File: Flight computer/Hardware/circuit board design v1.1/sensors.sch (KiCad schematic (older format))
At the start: 10 parts, among them U1 IIS2MDC, U10 BMI088, U8 MS5607-02BA

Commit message: put in new acclerometers and 9dof sensor. Changed supplier from mouser to farnell and RS
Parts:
- removed C28, C29, C31, C33: 100nF, Capacitor_SMD:C_0603_1608Metric, symbol Device:C_Small
- removed C30: 220nF, Capacitor_SMD:C_0603_1608Metric, symbol Device:C_Small
- removed C32: 10uF, Capacitor_SMD:C_0603_1608Metric, symbol Device:C_Small
- removed U1: IIS2MDC, Package_LGA:LGA-12_2x2mm_P0.5mm, symbol flight-computer:IIS2MDC
- removed U10: BMI088, BMI088:PQFN50P450X300X100-16N, symbol BMI088:BMI088
- added C13, C18: 10uF, Capacitor_SMD:C_0603_1608Metric, symbol Device:C_Small
- added C14, C15, C16, C17, C25: 100nF, Capacitor_SMD:C_0603_1608Metric, symbol Device:C_Small
- added C24: 10nF, Capacitor_SMD:C_0603_1608Metric, symbol Device:C_Small
- added U1: LSM9DS1, Package_LGA:LGA-24L_3x3.5mm_P0.43mm, symbol Sensor_Motion:LSM9DS1
- added U?: H3LIS100DL, Package_DFN_QFN:QFN-16-1EP_3x3mm_P0.5mm_EP1.45x1.45mm, symbol flight-computer:H3LIS100DL
- U8: min_quantity (none) -> 1
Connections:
- net labels added: ACCL_INT1, ACCL_INT2
- net labels removed: ACCL_RDY, GYRO_RDY, MAG_RDY
- wire segments 77 -> 113
- no-connect marks 4 -> 1
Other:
- note added: "C24(10nF) must guarantee \n1 nF value under 11 V bias \ncondition"
- note added: "Capacitor C1 (100 nF) should be a \ncapacitor with low ESR value and should \nbe placed as near as possible to the C1 pin."
- note added: "Power supply decoupling capacitors \n(100 nF ceramic, 10 μF aluminum) should be \nplaced as near as possible to pin 14 of the \ndevice (common design practice)."
- note added: "Power supply decoupling capacitors \n(100 nF ceramic,10 μF Al) should be placed \nas near as possible to the supply pin of the \ndevice (common design practice)."
- note added: "The slave address for accl/gyro is \n11010111b(D7h) for Read and \n11010110b (D6h) for Write."
- note added: "The slave address for mag is \n00111101b (3Dh) for Read and \n00111100b (3Ch) for Write."
- note added: "The slave address(SAD) is dress 0011001b.\nSA0 is connected to voltage supply."
- note removed: "Power supply decoupling capacitors (100 nF ceramic, 10 μF aluminum)"
- moved on the sheet: C77, U8

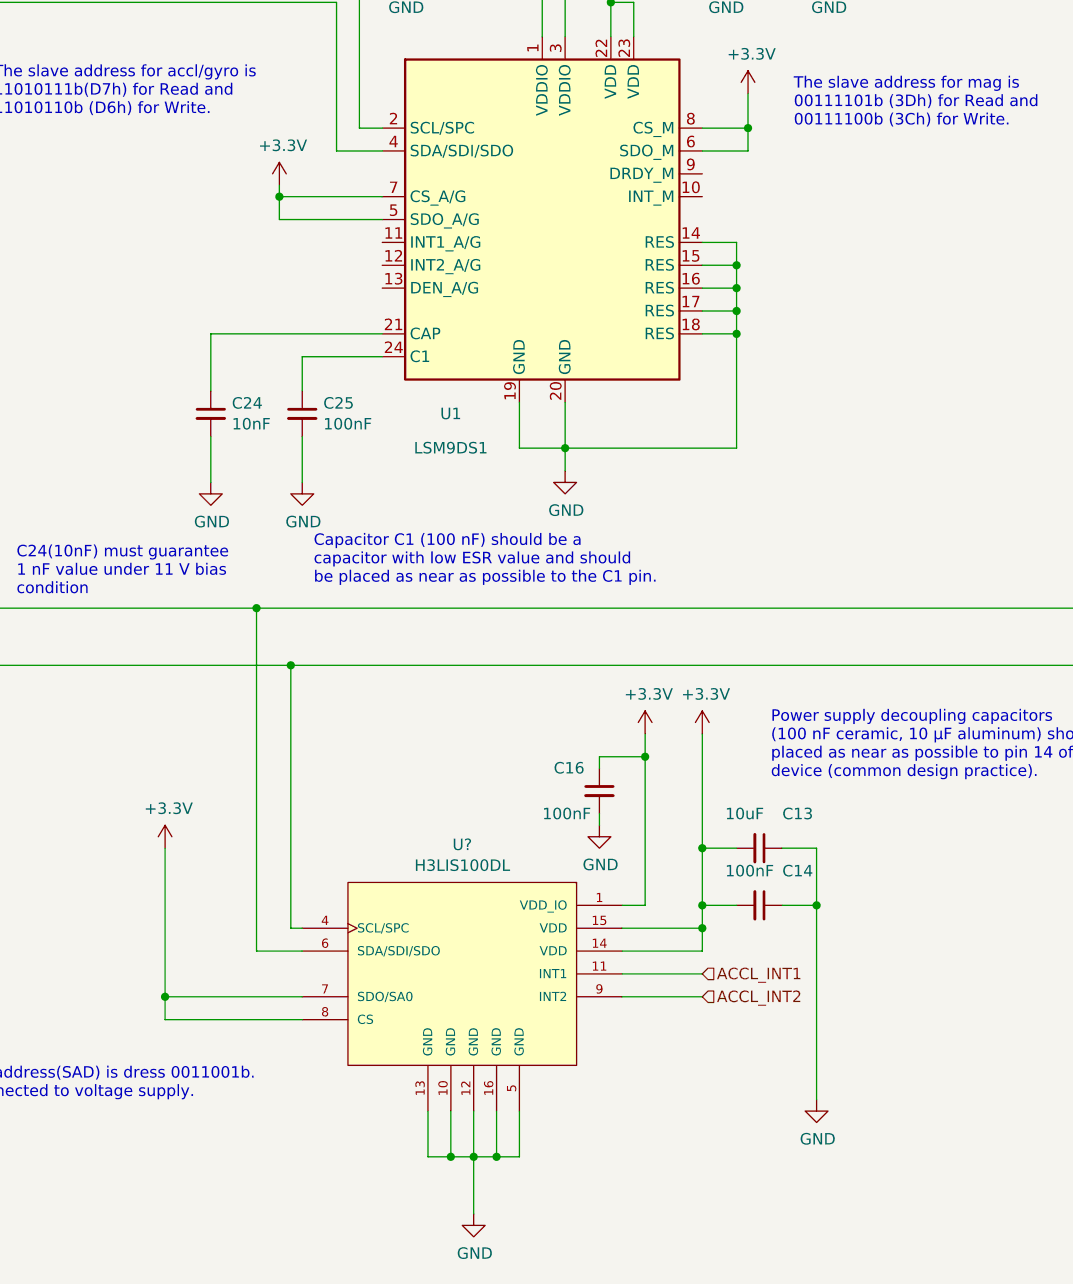
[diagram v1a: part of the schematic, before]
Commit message: wired up the news sensors
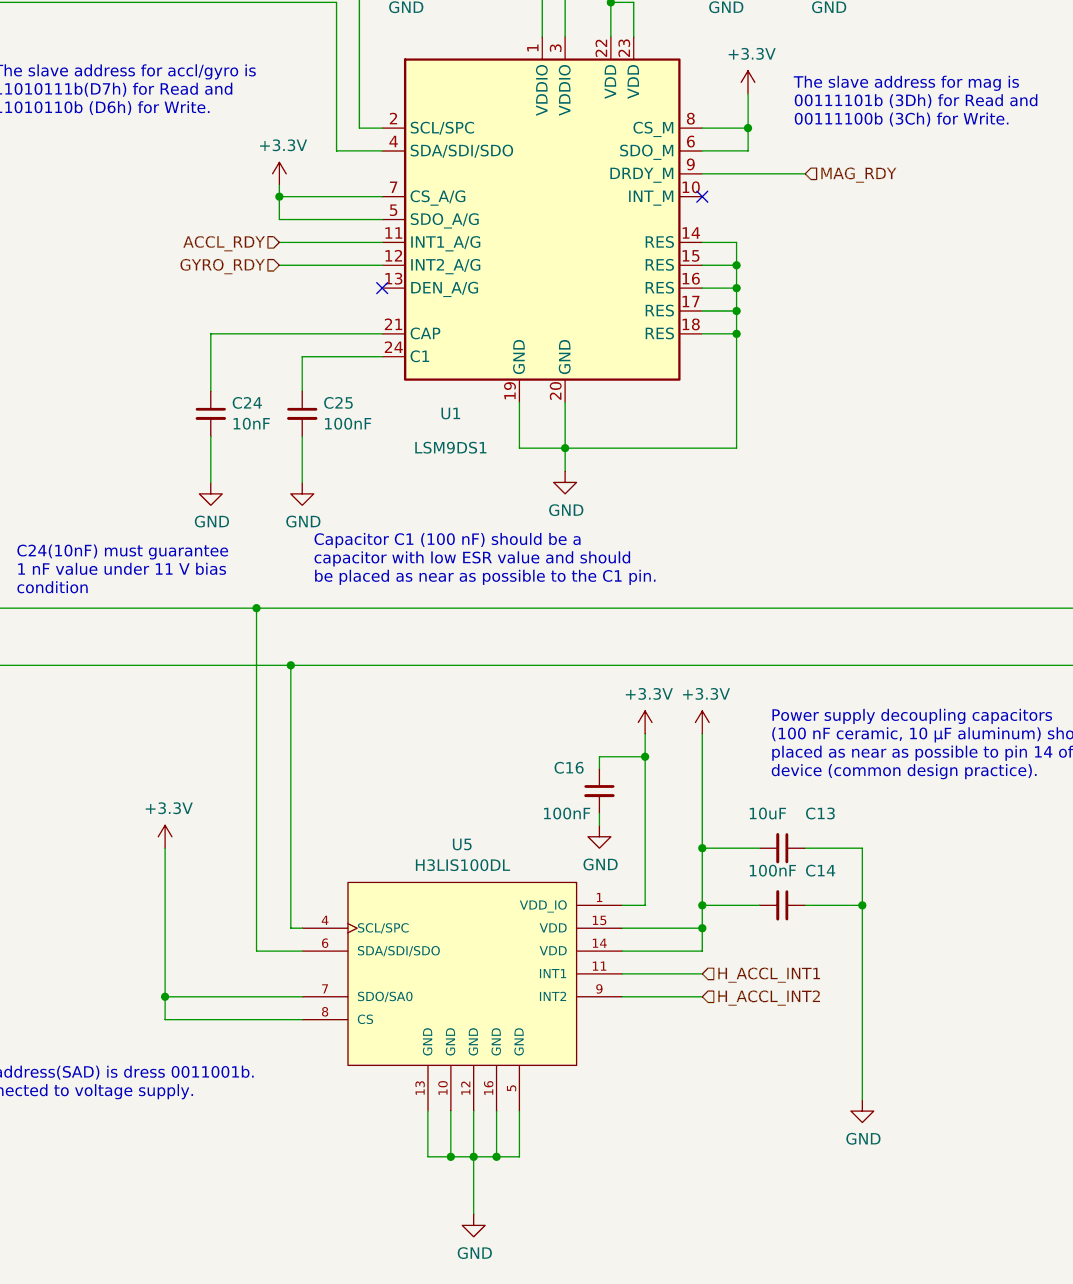
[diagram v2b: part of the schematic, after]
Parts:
- gave numbers to parts that had none: 1
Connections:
- net ACCL_RDY: now reaches U1.11 (INT1_A/G)
- net GYRO_RDY: now reaches U1.12 (INT2_A/G)
- net MAG_RDY: now reaches U1.9 (DRDY_M)
- net ACCL_INT1 renamed H_ACCL_INT1
- net ACCL_INT2 renamed H_ACCL_INT2
- no-connect marks 1 -> 3
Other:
- moved on the sheet: C13, C14
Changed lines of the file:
@@
 L power:GND #PWR017
 U 1 1 5D94C24A
-P 5700 6300
-F 0 "#PWR017" H 5700 6050 50  0001 C CNN
-F 1 "GND" H 5705 6127 50  0000 C CNN
-F 2 "" H 5700 6300 50  0001 C CNN
-F 3 "" H 5700 6300 50  0001 C CNN
-	1    5700 6300
+P 5900 6300
+F 0 "#PWR017" H 5900 6050 50  0001 C CNN
+F 1 "GND" H 5905 6127 50  0000 C CNN
+F 2 "" H 5900 6300 50  0001 C CNN
+F 3 "" H 5900 6300 50  0001 C CNN
+	1    5900 6300
 	1    0    0    -1
 $EndComp
@@
 L Device:C_Small C13
 U 1 1 5D94EBA2
-P 5450 5200
-F 0 "C13" V 5300 5300 50  0000 L CNN
-F 1 "10uF" V 5300 5050 50  0000 L CNN
-F 2 "Capacitor_SMD:C_0603_1608Metric" H 5450 5200 50  0001 C CNN
-F 3 "~" H 5450 5200 50  0001 C CNN
-	1    5450 5200
+P 5550 5200
+F 0 "C13" V 5400 5300 50  0000 L CNN
+F 1 "10uF" V 5400 5050 50  0000 L CNN
+F 2 "Capacitor_SMD:C_0603_1608Metric" H 5550 5200 50  0001 C CNN
+F 3 "~" H 5550 5200 50  0001 C CNN
+	1    5550 5200
 	0    1    1    0
 $EndComp
 Wire Wire Line
-	5200 5200 5350 5200
+	5200 5200 5450 5200
 Connection ~ 5200 5200
 Wire Wire Line
-	5550 5200 5700 5200
-Wire Wire Line
-	5700 5200 5700 5450
+	5650 5200 5900 5200
+Wire Wire Line
+	5900 5200 5900 5450
 $Comp
 L Device:C_Small C14
 U 1 1 5D951B11
-P 5450 5450
-F 0 "C14" V 5300 5550 50  0000 L CNN
-F 1 "100nF" V 5300 5300 50  0000 L CNN
-F 2 "Capacitor_SMD:C_0603_1608Metric" H 5450 5450 50  0001 C CNN
-F 3 "~" H 5450 5450 50  0001 C CNN
-	1    5450 5450
+P 5550 5450
+F 0 "C14" V 5400 5550 50  0000 L CNN
+F 1 "100nF" V 5400 5300 50  0000 L CNN
+F 2 "Capacitor_SMD:C_0603_1608Metric" H 5550 5450 50  0001 C CNN
+F 3 "~" H 5550 5450 50  0001 C CNN
+	1    5550 5450
 	0    1    1    0
 $EndComp
 Wire Wire Line
-	5200 5450 5350 5450
+	5200 5450 5450 5450
 Connection ~ 5200 5450
 Wire Wire Line
 	5200 5450 5200 5200
 Wire Wire Line
-	5550 5450 5700 5450
-Connection ~ 5700 5450
-Wire Wire Line
-	5700 5450 5700 6300
+	5650 5450 5900 5450
+Connection ~ 5900 5450
+Wire Wire Line
+	5900 5450 5900 6300
 Text Notes 5500 4900 0    50   ~ 0
 Power supply decoupling capacitors \n(100 nF ceramic, 10 μF aluminum) should be \nplaced as near as possible to pin 14 of the \ndevice (common design practice).
@@
 	4850 5450 4950 5450
 Text HLabel 5200 5750 2    50   Input ~ 0
-ACCL_INT1
+H_ACCL_INT1
 Wire Wire Line
 	4850 5750 5200 5750
 Text HLabel 5200 5850 2    50   Input ~ 0
-ACCL_INT2
+H_ACCL_INT2
 Wire Wire Line
 	5200 5850 4850 5850
@@
 C24(10nF) must guarantee \n1 nF value under 11 V bias \ncondition
 $Comp
-L flight-computer:H3LIS100DL U?
+L flight-computer:H3LIS100DL U5
 U 1 1 5D9FB40D
 P 4150 5750
-F 0 "U?" H 4150 6315 50  0000 C CNN
+F 0 "U5" H 4150 6315 50  0000 C CNN
 F 1 "H3LIS100DL" H 4150 6224 50  0000 C CNN
 F 2 "Package_DFN_QFN:QFN-16-1EP_3x3mm_P0.5mm_EP1.45x1.45mm" H 3550 6550 50  0001 L BNN
@@
 	3350 2350 3350 2300
 $Comp
-L power:+3.3V #PWR?
+L power:+3.3V #PWR046
 U 1 1 5DA31C3E
 P 3350 2300
-F 0 "#PWR?" H 3350 2150 50  0001 C CNN
+F 0 "#PWR046" H 3350 2150 50  0001 C CNN
 F 1 "+3.3V" H 3365 2473 50  0000 C CNN
 F 2 "" H 3350 2300 50  0001 C CNN
@@
 	5400 2050 5400 1900
 $Comp
-L power:+3.3V #PWR?
+L power:+3.3V #PWR047
 U 1 1 5DA4DC9B
 P 5400 1900
-F 0 "#PWR?" H 5400 1750 50  0001 C CNN
+F 0 "#PWR047" H 5400 1750 50  0001 C CNN
 F 1 "+3.3V" H 5415 2073 50  0000 C CNN
 F 2 "" H 5400 1900 50  0001 C CNN
@@
 Text Notes 5600 2050 0    50   ~ 0
 The slave address for mag is \n00111101b (3Dh) for Read and \n00111100b (3Ch) for Write.
+NoConn ~ 3800 2750
+Text HLabel 3350 2550 0    50   Input ~ 0
+ACCL_RDY
+Wire Wire Line
+	3800 2550 3350 2550
+Text HLabel 3350 2650 0    50   Input ~ 0
+GYRO_RDY
+Wire Wire Line
+	3800 2650 3350 2650
+Text HLabel 5650 2250 2    50   Input ~ 0
+MAG_RDY
+Wire Wire Line
+	5200 2250 5650 2250
+NoConn ~ 5200 2350
 $EndSCHEMATC

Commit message: Fully routed board v1.1 with the new high g accelerometer
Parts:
- U5: footprint Package_DFN_QFN:QFN-16-1EP_3x3mm_P0.5mm_EP1.45x1.45mm -> flight-computer:TFLGA-16_3x3mm
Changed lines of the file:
@@
 F 0 "U5" H 4150 6315 50  0000 C CNN
 F 1 "H3LIS100DL" H 4150 6224 50  0000 C CNN
-F 2 "Package_DFN_QFN:QFN-16-1EP_3x3mm_P0.5mm_EP1.45x1.45mm" H 3550 6550 50  0001 L BNN
+F 2 "flight-computer:TFLGA-16_3x3mm" H 3550 6550 50  0001 L BNN
 F 3 "https://docs-emea.rs-online.com/webdocs/14da/0900766b814da09a.pdf" H 3550 6550 50  0001 L BNN
 F 4 "2.47" H 4150 5750 50  0001 C CNN "Cost"

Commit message: put in logo for V1.1
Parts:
- C13, C18: Cost (none) -> 0.07; Purchase link (none) -> https://uk.rs-online.com/web/p/mlccs-multilayer-ceramic-cap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; min_quantity (none) -> 100
- C14, C15, C16, C17, C25: Cost (none) -> 0.01; Purchase link (none) -> https://uk.rs-online.com/web/p/mlccs-multilayer-ceramic-cap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; min_quantity (none) -> 50
- C24: Cost (none) -> 0.031; Purchase link (none) -> https://uk.rs-online.com/web/p/mlccs-multilayer-ceramic-cap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; min_quantity (none) -> 100
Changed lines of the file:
@@
 F 1 "10uF" V 5400 5050 50  0000 L CNN
 F 2 "Capacitor_SMD:C_0603_1608Metric" H 5550 5200 50  0001 C CNN
-F 3 "~" H 5550 5200 50  0001 C CNN
+F 3 "https://docs-emea.rs-online.com/webdocs/13b3/0900766b813b3e64.pdf" H 5550 5200 50  0001 C CNN
+F 4 "0.07" H 5550 5200 50  0001 C CNN "Cost"
+F 5 "https://uk.rs-online.com/web/p/mlccs-multilayer-ceramic-capacitors/8467293/" H 5550 5200 50  0001 C CNN "Purchase link"
+F 6 "100" H 5550 5200 50  0001 C CNN "min_quantity"
 	1    5550 5200
 	0    1    1    0
@@
 F 1 "100nF" V 5400 5300 50  0000 L CNN
 F 2 "Capacitor_SMD:C_0603_1608Metric" H 5550 5450 50  0001 C CNN
-F 3 "~" H 5550 5450 50  0001 C CNN
+F 3 "https://docs-emea.rs-online.com/webdocs/0dc2/0900766b80dc2409.pdf" H 5550 5450 50  0001 C CNN
+F 4 "0.01" H 5550 5450 50  0001 C CNN "Cost"
+F 5 "https://uk.rs-online.com/web/p/mlccs-multilayer-ceramic-capacitors/6983251/" H 5550 5450 50  0001 C CNN "Purchase link"
+F 6 "50" H 5550 5450 50  0001 C CNN "min_quantity"
 	1    5550 5450
 	0    1    1    0
@@
 F 1 "100nF" H 3992 1155 50  0000 L CNN
 F 2 "Capacitor_SMD:C_0603_1608Metric" H 3900 1200 50  0001 C CNN
-F 3 "~" H 3900 1200 50  0001 C CNN
+F 3 "https://docs-emea.rs-online.com/webdocs/0dc2/0900766b80dc2409.pdf" H 3900 1200 50  0001 C CNN
+F 4 "0.01" H 3900 1200 50  0001 C CNN "Cost"
+F 5 "https://uk.rs-online.com/web/p/mlccs-multilayer-ceramic-capacitors/6983251/" H 3900 1200 50  0001 C CNN "Purchase link"
+F 6 "50" H 3900 1200 50  0001 C CNN "min_quantity"
 	1    3900 1200
 	1    0    0    -1
@@
 F 1 "100nF" H 4500 4850 50  0000 L CNN
 F 2 "Capacitor_SMD:C_0603_1608Metric" H 4750 4950 50  0001 C CNN
-F 3 "~" H 4750 4950 50  0001 C CNN
+F 3 "https://docs-emea.rs-online.com/webdocs/0dc2/0900766b80dc2409.pdf" H 4750 4950 50  0001 C CNN
+F 4 "0.01" H 4750 4950 50  0001 C CNN "Cost"
+F 5 "https://uk.rs-online.com/web/p/mlccs-multilayer-ceramic-capacitors/6983251/" H 4750 4950 50  0001 C CNN "Purchase link"
+F 6 "50" H 4750 4950 50  0001 C CNN "min_quantity"
 	1    4750 4950
 	1    0    0    -1
@@
 F 1 "100nF" H 5392 1105 50  0000 L CNN
 F 2 "Capacitor_SMD:C_0603_1608Metric" H 5300 1150 50  0001 C CNN
-F 3 "~" H 5300 1150 50  0001 C CNN
+F 3 "https://docs-emea.rs-online.com/webdocs/0dc2/0900766b80dc2409.pdf" H 5300 1150 50  0001 C CNN
+F 4 "0.01" H 5300 1150 50  0001 C CNN "Cost"
+F 5 "https://uk.rs-online.com/web/p/mlccs-multilayer-ceramic-capacitors/6983251/" H 5300 1150 50  0001 C CNN "Purchase link"
+F 6 "50" H 5300 1150 50  0001 C CNN "min_quantity"
 	1    5300 1150
 	1    0    0    -1
@@
 F 1 "10uF" H 5842 1105 50  0000 L CNN
 F 2 "Capacitor_SMD:C_0603_1608Metric" H 5750 1150 50  0001 C CNN
-F 3 "~" H 5750 1150 50  0001 C CNN
+F 3 "https://docs-emea.rs-online.com/webdocs/13b3/0900766b813b3e64.pdf" H 5750 1150 50  0001 C CNN
+F 4 "0.07" H 5750 1150 50  0001 C CNN "Cost"
+F 5 "https://uk.rs-online.com/web/p/mlccs-multilayer-ceramic-capacitors/8467293/" H 5750 1150 50  0001 C CNN "Purchase link"
+F 6 "100" H 5750 1150 50  0001 C CNN "min_quantity"
 	1    5750 1150
 	1    0    0    -1
@@
 F 2 "Capacitor_SMD:C_0603_1608Metric" H 3050 3300 50  0001 C CNN
 F 3 "~" H 3050 3300 50  0001 C CNN
+F 4 "0.031" H 3050 3300 50  0001 C CNN "Cost"
+F 5 "https://uk.rs-online.com/web/p/mlccs-multilayer-ceramic-capacitors/8391727/" H 3050 3300 50  0001 C CNN "Purchase link"
+F 6 "100" H 3050 3300 50  0001 C CNN "min_quantity"
 	1    3050 3300
 	1    0    0    -1
@@
 F 1 "100nF" H 3542 3255 50  0000 L CNN
 F 2 "Capacitor_SMD:C_0603_1608Metric" H 3450 3300 50  0001 C CNN
-F 3 "~" H 3450 3300 50  0001 C CNN
+F 3 "https://docs-emea.rs-online.com/webdocs/0dc2/0900766b80dc2409.pdf" H 3450 3300 50  0001 C CNN
+F 4 "0.01" H 3450 3300 50  0001 C CNN "Cost"
+F 5 "https://uk.rs-online.com/web/p/mlccs-multilayer-ceramic-capacitors/6983251/" H 3450 3300 50  0001 C CNN "Purchase link"
+F 6 "50" H 3450 3300 50  0001 C CNN "min_quantity"
 	1    3450 3300
 	1    0    0    -1

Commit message: added in grove connector for break out pins. Made a new software framework for SAMD
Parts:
- added R4, R8: 4.7K, Resistor_SMD:R_0603_1608Metric, symbol Device:R
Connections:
- net +3V3: now also R4.1, R8.1
- net SENS_SCL: now also R8.2
- net SENS_SDA: now also R4.2
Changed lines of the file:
@@
 Connection ~ 3400 4400
 Wire Wire Line
-	3400 4400 8700 4400
+	3400 4400 7800 4400
 Wire Wire Line
 	3450 5650 3250 5650
@@
 Connection ~ 3250 4150
 Wire Wire Line
-	3250 4150 8850 4150
+	3250 4150 7500 4150
 Wire Wire Line
 	4850 5550 5200 5550
@@
 	5200 2250 5650 2250
 NoConn ~ 5200 2350
+Wire Wire Line
+	7500 3100 7500 3450
+Connection ~ 7500 4150
+Wire Wire Line
+	7500 4150 8850 4150
+Wire Wire Line
+	7800 4400 7800 3750
+Connection ~ 7800 4400
+Wire Wire Line
+	7800 4400 8700 4400
+$Comp
+L power:+3.3V #PWR048
+U 1 1 5D93D3F3
+P 7500 3100
+F 0 "#PWR048" H 7500 2950 50  0001 C CNN
+F 1 "+3.3V" H 7515 3273 50  0000 C CNN
+F 2 "" H 7500 3100 50  0001 C CNN
+F 3 "" H 7500 3100 50  0001 C CNN
+	1    7500 3100
+	1    0    0    -1
+$EndComp
+$Comp
+L power:+3.3V #PWR049
+U 1 1 5D93D8A4
+P 7800 3100
+F 0 "#PWR049" H 7800 2950 50  0001 C CNN
+F 1 "+3.3V" H 7815 3273 50  0000 C CNN
+F 2 "" H 7800 3100 50  0001 C CNN
+F 3 "" H 7800 3100 50  0001 C CNN
+	1    7800 3100
+	1    0    0    -1
+$EndComp
+$Comp
+L Device:R R4
+U 1 1 5D93DCCD
+P 7500 3600
+F 0 "R4" H 7570 3646 50  0000 L CNN
+F 1 "4.7K" H 7570 3555 50  0000 L CNN
+F 2 "Resistor_SMD:R_0603_1608Metric" V 7430 3600 50  0001 C CNN
+F 3 "~" H 7500 3600 50  0001 C CNN
+	1    7500 3600
+	1    0    0    -1
+$EndComp
+Wire Wire Line
+	7500 3750 7500 4150
+$Comp
+L Device:R R8
+U 1 1 5D93E817
+P 7800 3600
+F 0 "R8" H 7870 3646 50  0000 L CNN
+F 1 "4.7K" H 7870 3555 50  0000 L CNN
+F 2 "Resistor_SMD:R_0603_1608Metric" V 7730 3600 50  0001 C CNN
+F 3 "~" H 7800 3600 50  0001 C CNN
+	1    7800 3600
+	1    0    0    -1
+$EndComp
+Wire Wire Line
+	7800 3450 7800 3100
 $EndSCHEMATC

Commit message: updated links to purchase
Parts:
- C77: Cost (none) -> 0.003; Purchase link (none) -> https://uk.rs-online.com/web/p/mlccs-multilayer-ceramic-cap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; min_quantity (none) -> 50
- R4, R8: Cost (none) -> 0.01; Purchase link (none) -> https://uk.rs-online.com/web/p/surface-mount-fixed-resistor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; min_quantity (none) -> 50
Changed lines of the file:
@@
 F 2 "Capacitor_SMD:C_0603_1608Metric" H 9900 4900 50  0001 C CNN
 F 3 "~" H 9900 4900 50  0001 C CNN
+F 4 "0.003" H 9900 4900 50  0001 C CNN "Cost"
+F 5 "https://uk.rs-online.com/web/p/mlccs-multilayer-ceramic-capacitors/0391135/" H 9900 4900 50  0001 C CNN "Purchase link"
+F 6 "50" H 9900 4900 50  0001 C CNN "min_quantity"
 	1    9900 4900
 	1    0    0    -1
@@
 F 2 "Resistor_SMD:R_0603_1608Metric" V 7430 3600 50  0001 C CNN
 F 3 "~" H 7500 3600 50  0001 C CNN
+F 4 "0.01" H 7500 3600 50  0001 C CNN "Cost"
+F 5 "https://uk.rs-online.com/web/p/surface-mount-fixed-resistors/7408877/" H 7500 3600 50  0001 C CNN "Purchase link"
+F 6 "50" H 7500 3600 50  0001 C CNN "min_quantity"
 	1    7500 3600
 	1    0    0    -1
@@
 F 2 "Resistor_SMD:R_0603_1608Metric" V 7730 3600 50  0001 C CNN
 F 3 "~" H 7800 3600 50  0001 C CNN
+F 4 "0.01" H 7800 3600 50  0001 C CNN "Cost"
+F 5 "https://uk.rs-online.com/web/p/surface-mount-fixed-resistors/7408877/" H 7800 3600 50  0001 C CNN "Purchase link"
+F 6 "50" H 7800 3600 50  0001 C CNN "min_quantity"
 	1    7800 3600
 	1    0    0    -1
